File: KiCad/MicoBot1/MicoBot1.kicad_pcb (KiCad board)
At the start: 2 copper layers, 50 x 50 mm, 21 parts, among them J1 Prog, J2 Bat, J3 Motor2, J4 Motor1, J5 Datos, J6 Vcc, J7 Gnd, SW1 Rst, SW2 On, U1 ATmega328P-PU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

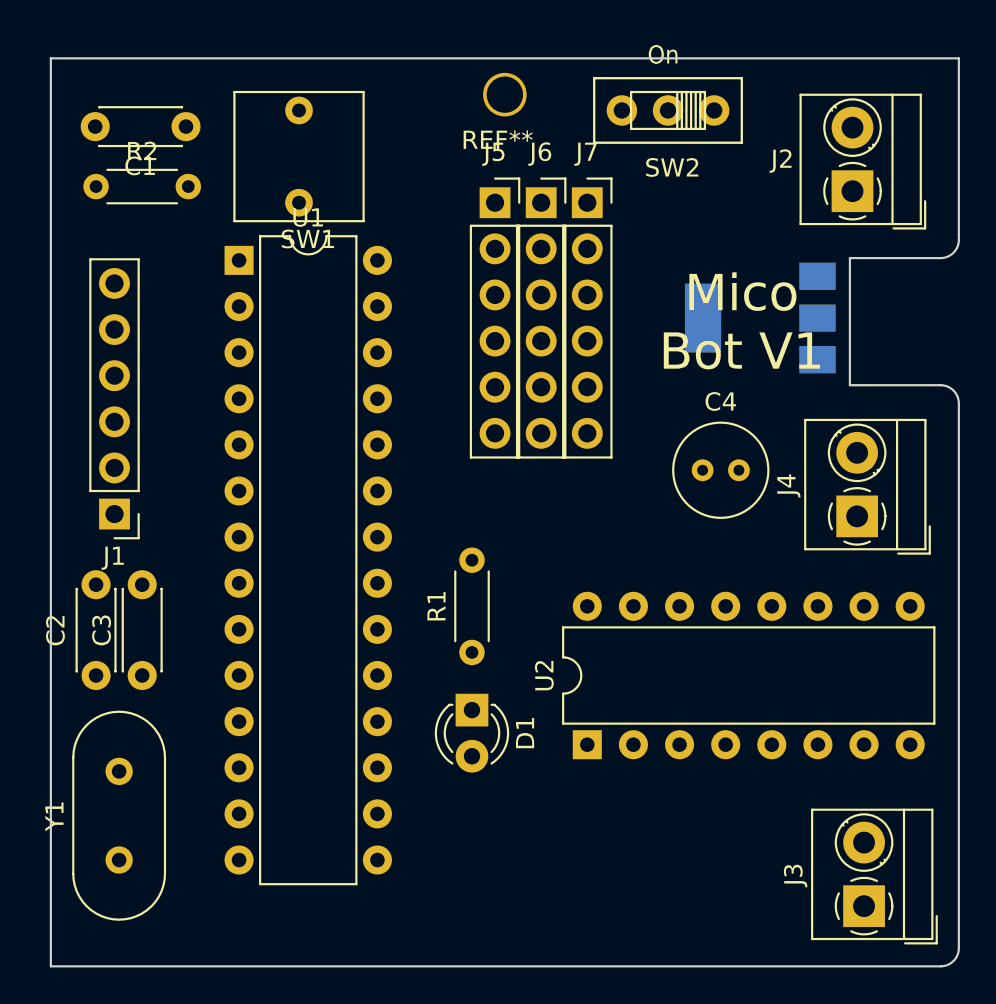
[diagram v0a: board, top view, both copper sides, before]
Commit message: 
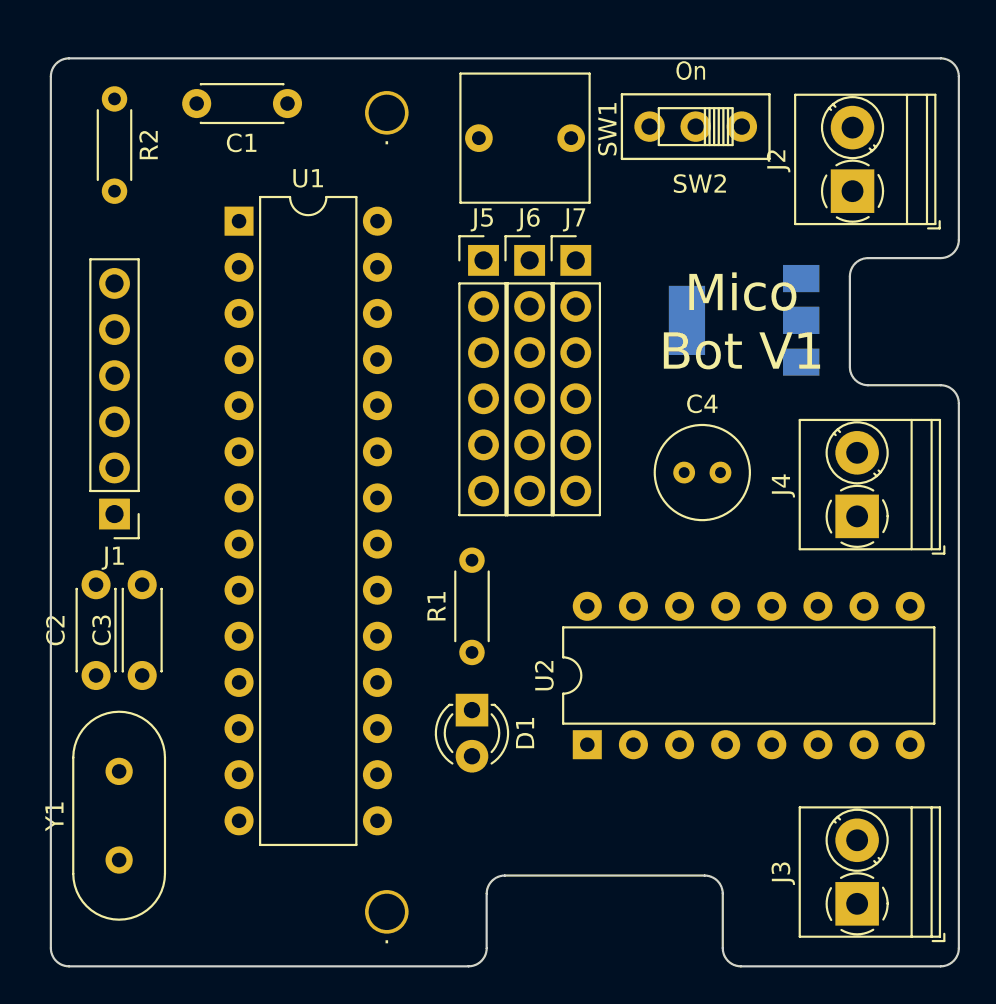
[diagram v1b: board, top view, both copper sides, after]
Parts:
- added .: ., MiLib:Taladro_2mm, F.Cu at (118.5, 147.0)
- .: renamed from REF**; value Taladro_2mm -> .
- J2, J3, J4: footprint TerminalBlock_MetzConnect:TerminalBlock_MetzConnect_Type059_RT06302HBWC_1x02_P3.50mm_Horizontal -> TerminalBlock_Phoenix:TerminalBlock_Phoenix_PT-1,5-2-3.5-H_1x02_P3.50mm_Horizontal
- J5, J6, J7: footprint Connector_PinSocket_2.54mm:PinSocket_1x06_P2.54mm_Vertical -> Connector_PinHeader_2.54mm:PinHeader_1x06_P2.54mm_Vertical
- moved SW1 10.5 mm to (126.1, 101.9), turned to 0 degrees
- moved . 6.50 mm to (118.5, 103.0)
- moved C1 5.73 mm to (113.0, 102.5)
- moved R2 4.93 mm to (103.5, 102.2), turned to 270 degrees
- moved J6 3.24 mm to (126.4, 111.1)
- moved J5 3.24 mm to (123.8, 111.1)
- moved J7 3.24 mm to (128.9, 111.1)
- moved U1 2.16 mm to (110.4, 109.0)
- moved SW2 1.76 mm to (135.5, 103.8)
- moved C4 1.02 mm to (134.9, 122.8)
- moved U3 0.90 mm to (138.2, 114.4)
- moved J3 0.40 mm to (144.4, 146.6)
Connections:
- U1 pad 4: Net-(U1-Pad4) -> Net-(J1-Pad5)
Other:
- outline, holes or cut-outs redrawn

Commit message: 
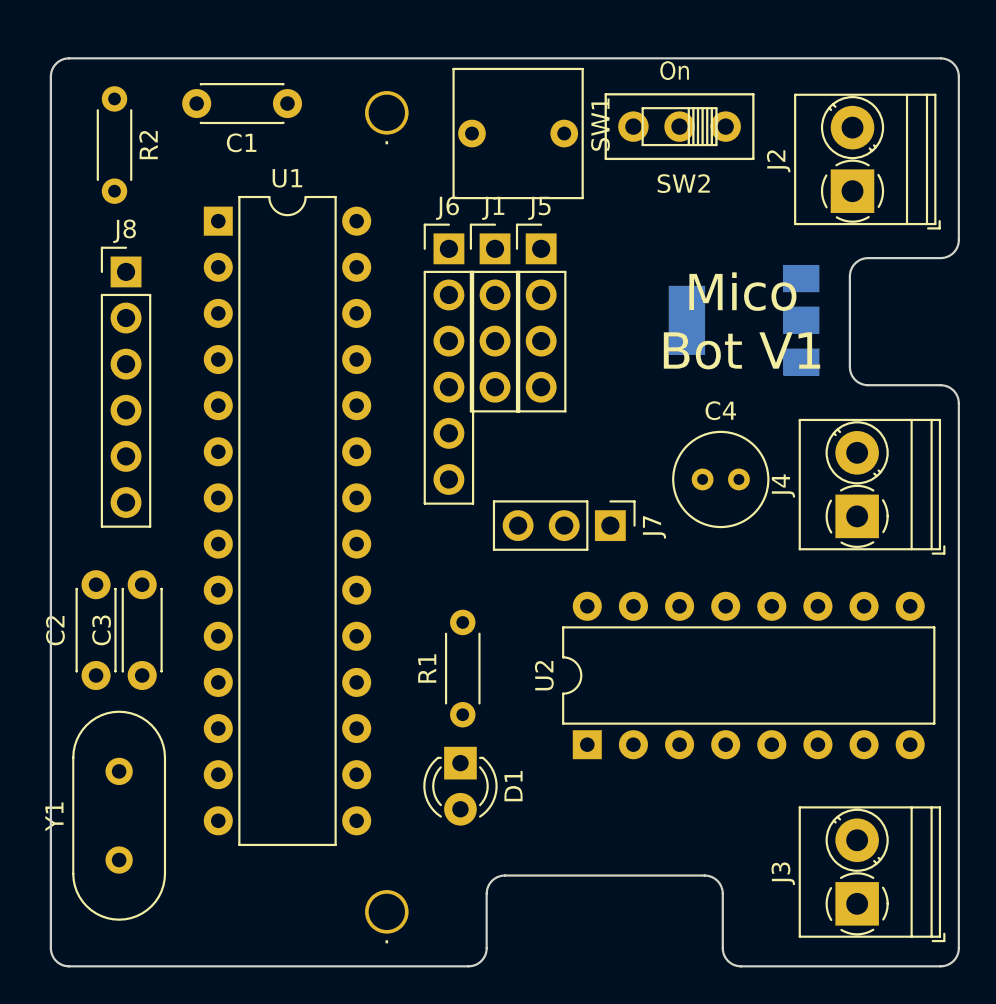
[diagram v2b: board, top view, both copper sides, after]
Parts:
- added J8: Conn_01x06_Male, Connector_PinHeader_2.54mm:PinHeader_1x06_P2.54mm_Vertical, F.Cu at (104.1, 111.8)
- J1: value Prog -> Conn_01x04_Male; footprint Connector_PinHeader_2.54mm:PinHeader_1x06_P2.54mm_Vertical -> Connector_PinHeader_2.54mm:PinHeader_1x04_P2.54mm_Vertical
- J5: value Datos -> Conn_01x04_Male; footprint Connector_PinHeader_2.54mm:PinHeader_1x06_P2.54mm_Vertical -> Connector_PinHeader_2.54mm:PinHeader_1x04_P2.54mm_Vertical
- J6: value Vcc -> Conn_01x06_Male
- J7: value Gnd -> Conn_01x03_Male; footprint Connector_PinHeader_2.54mm:PinHeader_1x06_P2.54mm_Vertical -> Connector_PinHeader_2.54mm:PinHeader_1x03_P2.54mm_Vertical
- moved J1 25.5 mm to (124.5, 110.5), turned to 0 degrees
- moved J7 14.7 mm to (130.8, 125.7), turned to 270 degrees
- moved J6 4.49 mm to (121.9, 110.5)
- moved R1 3.47 mm to (122.7, 136.1)
- moved J5 3.24 mm to (127.0, 110.5)
- moved D1 2.99 mm to (122.6, 138.8)
- moved U1 1.14 mm to (109.2, 109.0)
- moved C4 1.09 mm to (135.9, 123.2)
- moved SW2 0.89 mm to (134.6, 103.8)
- moved SW1 0.46 mm to (125.7, 101.6)
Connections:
- J1 pad 1: Net-(C1-Pad2) -> VCC
- J1 pad 2: Net-(J1-Pad2) -> VCC
- J1 pad 3: Net-(J1-Pad3) -> VCC
- J5 pad 1: Net-(J5-Pad1) -> GND
- J5 pad 2: Net-(J5-Pad2) -> GND
- J5 pad 3: Net-(J5-Pad3) -> GND
- J5 pad 4: Net-(J5-Pad4) -> GND
- J6 pad 1: VCC -> Net-(J6-Pad1)
- J6 pad 2: VCC -> Net-(J6-Pad2)
- J6 pad 3: VCC -> Net-(J6-Pad3)
- J6 pad 4: VCC -> Net-(J6-Pad4)
- J6 pad 5: VCC -> Net-(J6-Pad5)
- J6 pad 6: VCC -> Net-(J6-Pad6)
- J7 pad 1: GND -> Net-(J7-Pad1)
- J7 pad 2: GND -> Net-(J7-Pad2)
- J7 pad 3: GND -> Net-(J7-Pad3)
- U1 pad 2: Net-(J1-Pad3) -> Net-(J8-Pad4)
- U1 pad 23: Net-(J5-Pad6) -> Net-(J6-Pad6)
- U1 pad 24: Net-(J5-Pad5) -> Net-(J6-Pad5)
- U1 pad 25: Net-(J5-Pad4) -> Net-(J6-Pad4)
- U1 pad 26: Net-(J5-Pad3) -> Net-(J6-Pad3)
- U1 pad 27: Net-(J5-Pad2) -> Net-(J6-Pad2)
- U1 pad 28: Net-(J5-Pad1) -> Net-(J6-Pad1)
- U1 pad 3: Net-(J1-Pad2) -> Net-(J8-Pad5)
- U1 pad 4: Net-(J1-Pad5) -> Net-(J7-Pad1)
- U1 pad 5: Net-(U1-Pad5) -> Net-(J7-Pad2)
- U1 pad 6: Net-(U1-Pad6) -> Net-(J7-Pad3)

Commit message: 
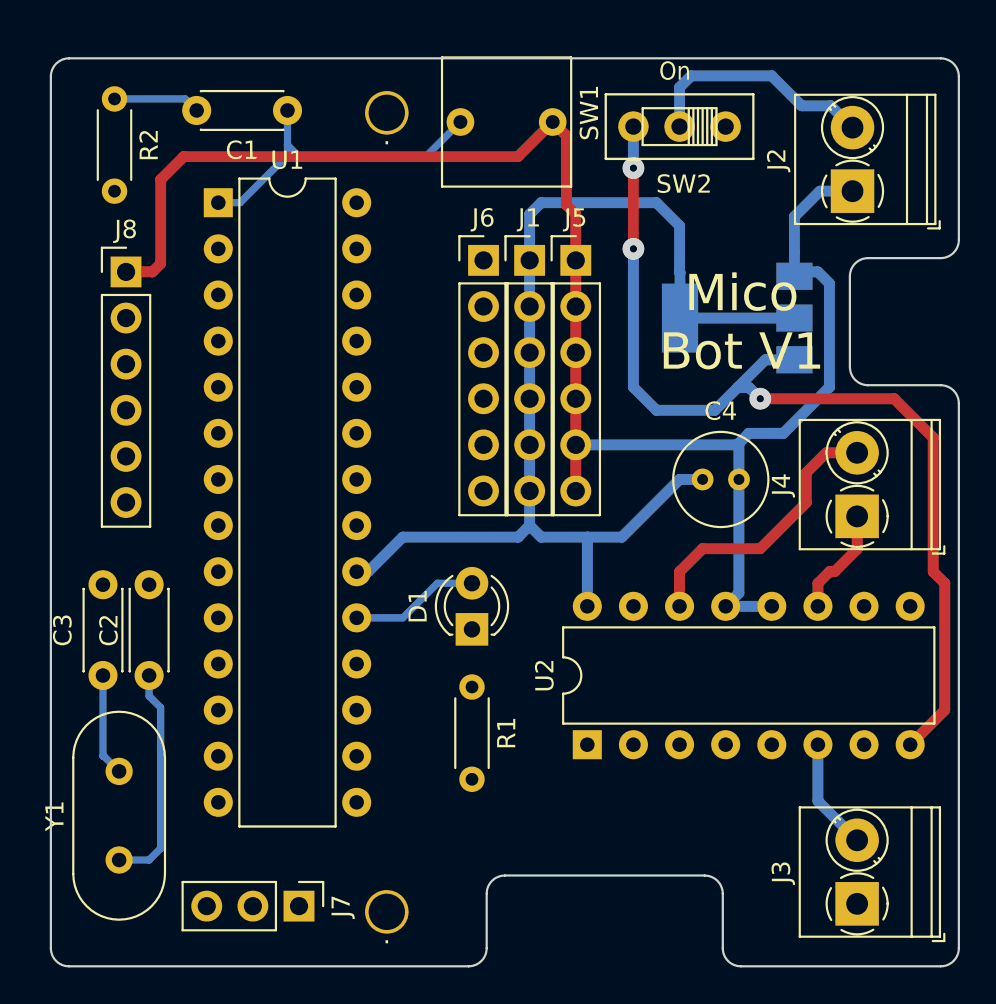
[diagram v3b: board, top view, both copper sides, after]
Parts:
- J1: value Conn_01x04_Male -> +5v; footprint Connector_PinHeader_2.54mm:PinHeader_1x04_P2.54mm_Vertical -> Connector_PinHeader_2.54mm:PinHeader_1x06_P2.54mm_Vertical
- J5: value Conn_01x04_Male -> GND; footprint Connector_PinHeader_2.54mm:PinHeader_1x04_P2.54mm_Vertical -> Connector_PinHeader_2.54mm:PinHeader_1x06_P2.54mm_Vertical
- J6: value Conn_01x06_Male -> ANin
- J7: value Conn_01x03_Male -> Din
- J8: value Conn_01x06_Male -> Serial
- moved J7 27.1 mm to (113.7, 146.7)
- moved D1 7.39 mm to (123.2, 131.4), turned to 90 degrees
- moved C2 2.92 mm to (105.4, 134.0)
- moved C3 2.16 mm to (102.9, 134.0)
- moved J1 2.01 mm to (126.4, 111.1)
- moved J5 2.01 mm to (128.9, 111.1)
- moved J6 2.01 mm to (123.8, 111.1)
- moved R1 1.61 mm to (123.2, 134.6), turned to 270 degrees
- moved U1 1.02 mm to (109.2, 108.0)
- moved SW1 0.90 mm to (125.1, 101.0)
- moved U3 0.40 mm to (137.8, 114.3)
- moved C1 0.38 mm to (113.0, 102.9)
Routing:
- net GND: track 0.00 -> 92.7 mm
- net VCC: track 0.00 -> 63.1 mm
- net VSS: track 0.00 -> 54.8 mm, vias 0 -> 3
- net Net-(C1-Pad1): track 0.00 -> 17.9 mm
- net Net-(J4-Pad2): track 0.00 -> 15.4 mm
- net Net-(J2-Pad2): track 0.00 -> 13.1 mm
- net Net-(C2-Pad1): track 0.00 -> 12.3 mm
- net Net-(D1-Pad2): track 0.00 -> 7.14 mm
- net Net-(J3-Pad2): track 0.00 -> 6.16 mm
- net Net-(J4-Pad1): track 0.00 -> 6.01 mm
- net Net-(C3-Pad1): track 0.00 -> 5.68 mm
- net Net-(C1-Pad2): track 0.00 -> 4.79 mm
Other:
- net class Default: clearance 0.2 -> 0.25; trace_width 0.25 -> 0.4; via_dia 0.8 -> 1
- net class Potencia added: clearance 0.25, trace_width 0.6, via_dia 1.2, via_drill 0.4
- rule trace_clearance: 0.2 -> 0.25

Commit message: 
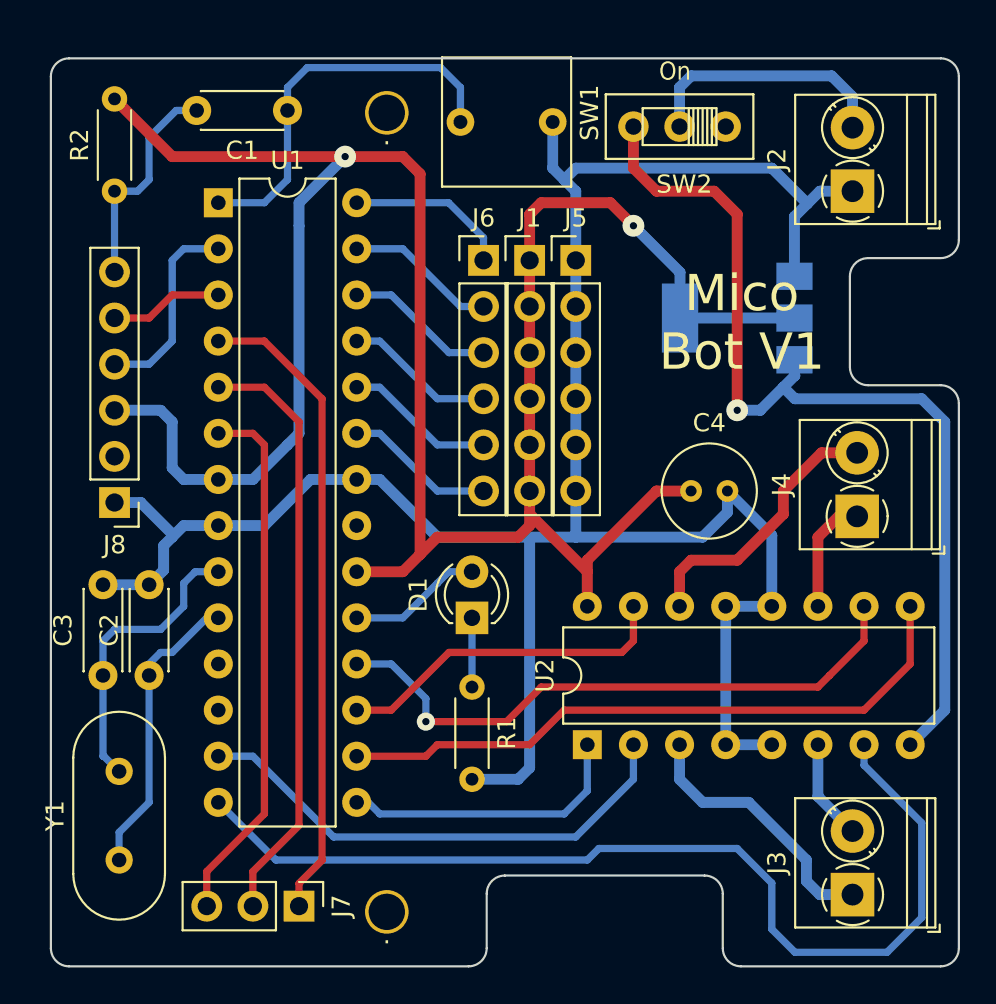
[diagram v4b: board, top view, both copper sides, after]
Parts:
- moved J8 12.7 mm to (103.5, 124.5), turned to 180 degrees
- moved R2 5.08 mm to (103.5, 107.3), turned to 90 degrees
- moved C4 0.90 mm to (135.3, 123.8)
- moved D1 0.63 mm to (123.2, 130.8)
- moved J3 0.57 mm to (144.1, 146.1)
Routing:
- net VCC: track 63.1 -> 131.1 mm, vias 0 -> 2
- net Net-(U1-Pad14): track 0.00 -> 55.8 mm
- net Net-(U1-Pad16): track 0.00 -> 35.8 mm
- net Net-(J7-Pad1): track 0.00 -> 35.5 mm
- net Net-(U1-Pad18): track 0.00 -> 33.7 mm, vias 0 -> 1
- net GND: track 92.7 -> 125.8 mm
- net Net-(J7-Pad2): track 0.00 -> 33.0 mm
- net Net-(J7-Pad3): track 0.00 -> 29.5 mm
- net Net-(U1-Pad13): track 0.00 -> 27.9 mm
- net Net-(U1-Pad17): track 0.00 -> 18.7 mm
- net Net-(U1-Pad15): track 0.00 -> 16.0 mm
- net Net-(J3-Pad1): track 0.00 -> 14.7 mm
- net Net-(J8-Pad4): track 0.00 -> 10.9 mm
- net Net-(C3-Pad1): track 5.68 -> 16.3 mm
- net Net-(J6-Pad1): track 0.00 -> 9.03 mm
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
